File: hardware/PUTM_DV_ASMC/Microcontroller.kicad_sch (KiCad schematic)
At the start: 25 parts, among them U5 LM4040C33FTA, U6 STM32G484RETx

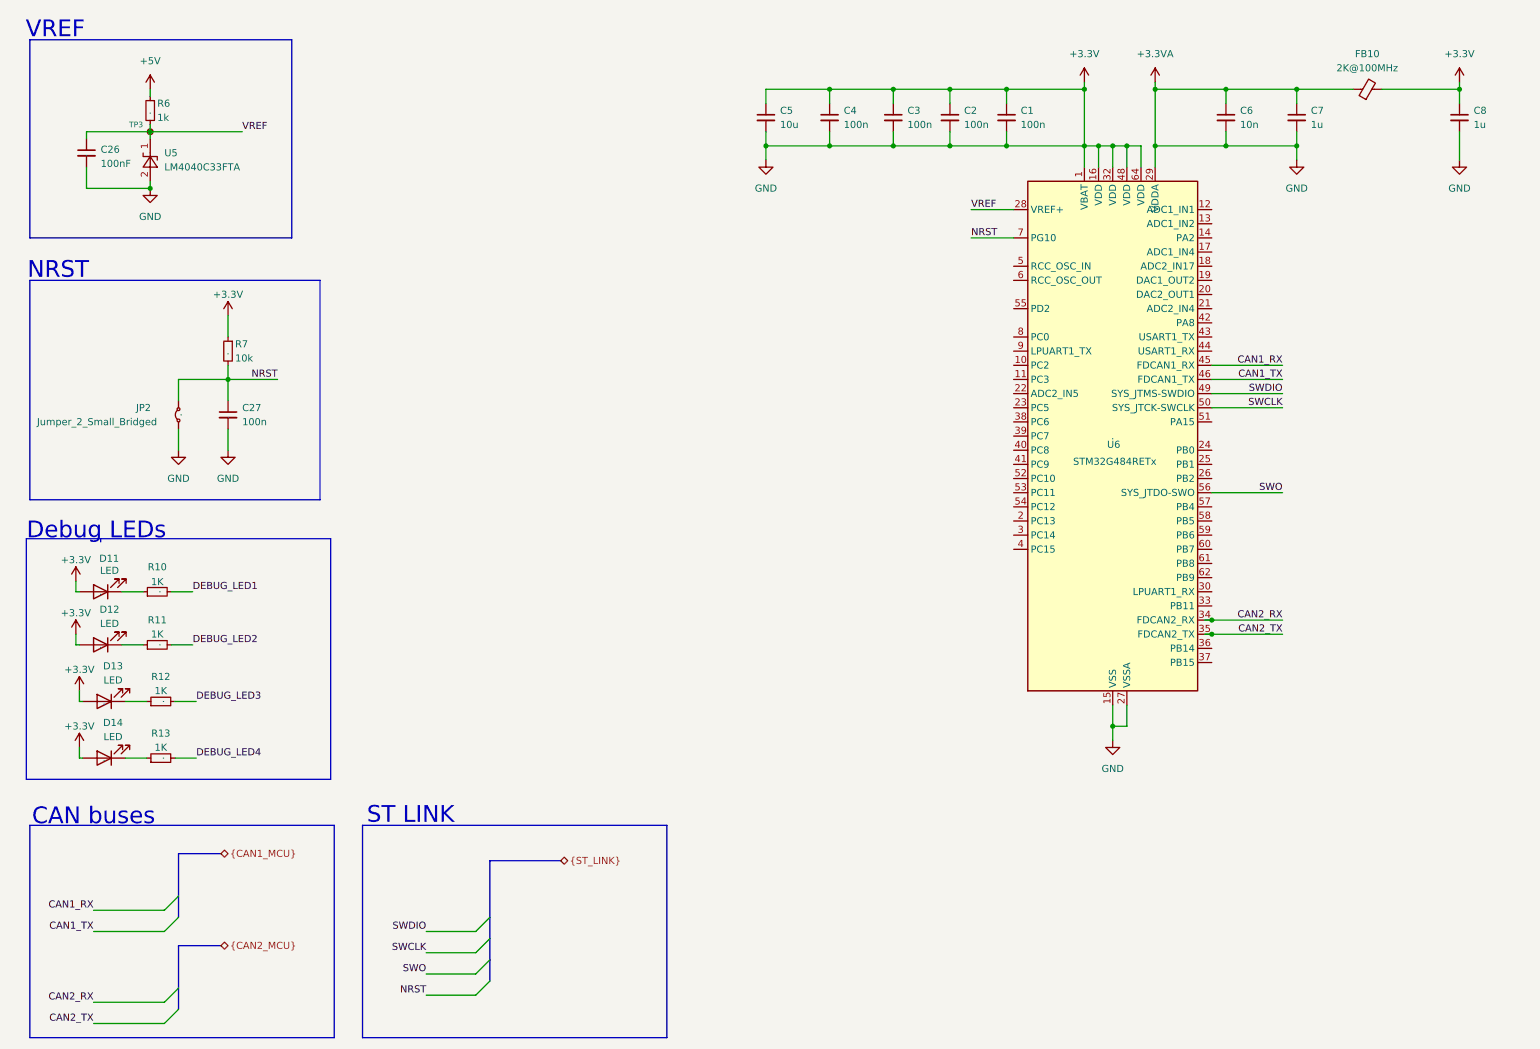
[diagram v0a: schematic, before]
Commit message: schematics without main connector
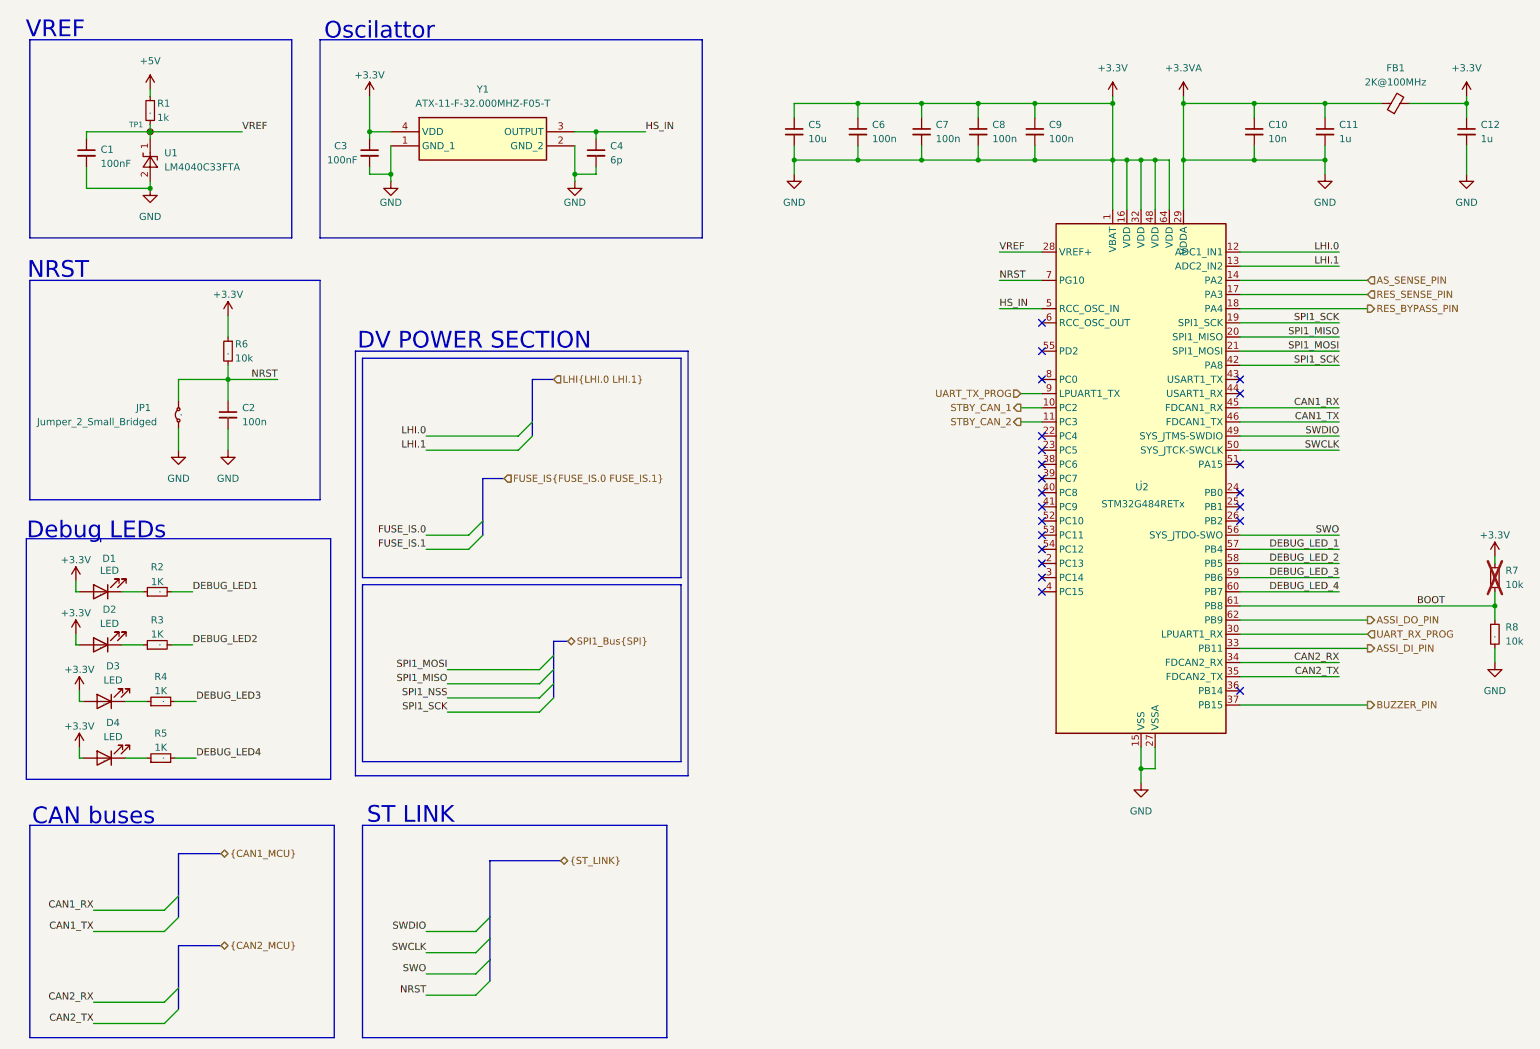
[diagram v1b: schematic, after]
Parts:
- added C3: 100nF, Capacitor_SMD:C_0603_1608Metric_Pad1.08x0.95mm_HandSolder, symbol Device:C_Small
- added C4: 6p, Capacitor_SMD:C_0603_1608Metric_Pad1.08x0.95mm_HandSolder, symbol Device:C_Small
- added R7, R8: 10k, Resistor_SMD:R_0603_1608Metric, symbol Device:R_Small
- added Y1: ATX-11-F-32.000MHZ-F05-T, Samacsys:ATX11F32000MHZF05T, symbol Samacsys:ATX-11-F-32.000MHZ-F05-T
- renumbered C26 to C1, C6 to C10, C7 to C11, C8 to C12, C27 to C2, C4 to C6, C3 to C7, C2 to C8, C1 to C9, D11 to D1, D12 to D2, D13 to D3, D14 to D4, FB10 to FB1, JP2 to JP1, R6 to R1, R10 to R2, R11 to R3, R12 to R4, R13 to R5, R7 to R6, TP3 to TP1, U5 to U1, U6 to U2
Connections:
- net +3.3V: now also C3.1, C3.2, C4.2, R7.1, R8.2, Y1.1 (GND_1), Y1.2 (GND_2), Y1.4 (VDD)
- net STBY_CAN_1: now reaches U2.10 (PC2)
- net STBY_CAN_2: now reaches U2.11 (PC3)
- net LHI.0: now reaches U2.12 (PA0)
- net LHI.1: now reaches U2.13 (PA1)
- net AS_SENSE_PIN: now reaches U2.14 (PA2)
- net RES_SENSE_PIN: now reaches U2.17 (PA3)
- net RES_BYPASS_PIN: now reaches U2.18 (PA4)
- net SPI1_SCK: now reaches U2.19 (PA5)
- net SPI1_SCK: now also U2.42 (PA8)
- net SPI1_MISO: now reaches U2.20 (PA6)
- net SPI1_MOSI: now reaches U2.21 (PA7)
- net UART_RX_PROG: now reaches U2.30 (PB10)
- net ASSI_DI_PIN: now reaches U2.33 (PB11)
- net BUZZER_PIN: now reaches U2.37 (PB15)
- net HS_IN: now reaches U2.5 (PF0)
- net HS_IN: now also C4.1, Y1.3 (OUTPUT)
- net DEBUG_LED_1: now reaches U2.57 (PB4)
- net DEBUG_LED_2: now reaches U2.58 (PB5)
- net DEBUG_LED_3: now reaches U2.59 (PB6)
- net DEBUG_LED_4: now reaches U2.60 (PB7)
- net BOOT: now reaches U2.61 (PB8)
- net BOOT: now also R7.2, R8.1
- net ASSI_DO_PIN: now reaches U2.62 (PB9)
- net UART_TX_PROG: now reaches U2.9 (PC1)
- no-connect marks 0 -> 22
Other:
- note added: "DV POWER SECTION"
- note added: "Oscilattor"
- moved on the sheet: C10, C11, C12, C5, C6, C7, C8, C9, FB1, U2

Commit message: done schematic v1
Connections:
- net ADC: now reaches U2.24 (PB0)
- net GPIO: now reaches U2.25 (PB1)
- no-connect marks 22 -> 20
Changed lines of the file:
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@@
 	)
 	(no_connect
-		(at 233.68 101.6)
-	)
-	(no_connect
 		(at 233.68 78.74)
 	)
@@
 	)
 	(no_connect
-		(at 233.68 99.06)
-	)
-	(no_connect
 		(at 198.12 111.76)
 	)
@@
 	(wire
 		(pts
+			(xy 233.68 99.06) (xy 256.54 99.06)
+		)
+		(stroke
+			(width 0)
+			(type default)
+		)
+	)
+	(wire
+		(pts
 			(xy 42.545 146.685) (xy 46.355 146.685)
 		)
@@
 	(wire
 		(pts
+			(xy 233.68 101.6) (xy 256.54 101.6)
+		)
+		(stroke
+			(width 0)
+			(type default)
+		)
+	)
+	(wire
+		(pts
 			(xy 38.1 35.56) (xy 38.1 34.29)
 		)
@@
 		)
 	)
+	(hierarchical_label "ADC"
+		(shape bidirectional)
+		(at 256.54 99.06 0)
+		(effects
+			(font
+				(size 1.27 1.27)
+			)
+			(justify left)
+		)
+	)
 	(hierarchical_label "RES_BYPASS_PIN"
 		(shape output)
@@
 	)
 	(hierarchical_label "ASSI_DI_PIN"
-		(shape output)
+		(shape bidirectional)
 		(at 256.54 127 0)
 		(effects
@@
 		)
 	)
+	(hierarchical_label "GPIO"
+		(shape bidirectional)
+		(at 256.54 101.6 0)
+		(effects
+			(font
+				(size 1.27 1.27)
+			)
+			(justify left)
+		)
+	)
 	(hierarchical_label "UART_RX_PROG"
 		(shape input)
@@
 		)
 		(property "Value" "STM32G484RETx"
-			(at 208.788 101.092 0)
+			(at 208.788 96.012 0)
 			(show_name no)
 			(do_not_autoplace no)
@@
 		)
 		(pin "25"
+			(alternate "ADC3_IN1")
 		)
 		(pin "56"

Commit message: schematic without error
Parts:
- Y1: footprint Samacsys:ATX11F32000MHZF05T -> ATX11F32000MHZF05T:ATX11F32000MHZF05T
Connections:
- net DEBUG_LED1 is gone; now on net DEBUG_LED_1: R2.2
- net DEBUG_LED2 is gone; now on net DEBUG_LED_2: R3.2
- net DEBUG_LED3 is gone; now on net DEBUG_LED_3: R4.2
- net DEBUG_LED4 is gone; now on net DEBUG_LED_4: R5.2
- net SPI1_NSS: now also U2.42 (PA8)
- net SPI1_SCK: no longer U2.42 (PA8)
- net FUSE_ISO.0: now reaches U2.40 (PC8)
- net FUSE_ISO.1: now reaches U2.41 (PC9)
- no-connect marks 20 -> 18
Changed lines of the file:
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@@
 	(rectangle
 		(start 74.93 73.66)
-		(end 134.62 149.86)
+		(end 137.16 149.86)
 		(stroke
 			(width 0)
@@
 	(rectangle
 		(start 76.2 115.57)
-		(end 133.35 147.32)
+		(end 135.89 147.32)
 		(stroke
 			(width 0)
@@
 	(rectangle
 		(start 76.2 74.93)
-		(end 133.35 114.3)
+		(end 135.89 114.3)
 		(stroke
 			(width 0)
@@
 	)
 	(no_connect
-		(at 198.12 101.6)
-	)
-	(no_connect
-		(at 198.12 99.06)
-	)
-	(no_connect
 		(at 198.12 78.74)
 	)
@@
 	(wire
 		(pts
+			(xy 190.5 99.06) (xy 198.12 99.06)
+		)
+		(stroke
+			(width 0)
+			(type default)
+		)
+	)
+	(wire
+		(pts
 			(xy 25.4 144.78) (xy 25.4 146.685)
 		)
@@
 	(wire
 		(pts
+			(xy 190.5 101.6) (xy 198.12 101.6)
+		)
+		(stroke
+			(width 0)
+			(type default)
+		)
+	)
+	(wire
+		(pts
 			(xy 26.035 146.685) (xy 25.4 146.685)
 		)
@@
 		)
 	)
+	(label "FUSE_ISO.0"
+		(at 190.5 99.06 180)
+		(effects
+			(font
+				(size 1.27 1.27)
+			)
+			(justify right bottom)
+		)
+	)
 	(label "CAN1_RX"
 		(at 27.94 173.99 180)
@@
 		)
 	)
-	(label "DEBUG_LED4"
+	(label "DEBUG_LED_4"
 		(at 46.355 146.685 0)
 		(effects
@@
 		)
 	)
-	(label "FUSE_IS.0"
+	(label "FUSE_ISO.0"
 		(at 87.63 106.68 180)
 		(effects
@@
 		)
 	)
-	(label "SPI1_SCK"
+	(label "SPI1_NSS"
 		(at 251.46 76.2 180)
 		(effects
@@
 		)
 	)
-	(label "DEBUG_LED1"
+	(label "DEBUG_LED_1"
 		(at 45.72 116.84 0)
 		(effects
@@
 		)
 	)
+	(label "FUSE_ISO.1"
+		(at 190.5 101.6 180)
+		(effects
+			(font
+				(size 1.27 1.27)
+			)
+			(justify right bottom)
+		)
+	)
 	(label "CAN2_TX"
 		(at 27.94 194.31 180)
@@
 		)
 	)
-	(label "DEBUG_LED3"
+	(label "DEBUG_LED_3"
 		(at 46.355 136.525 0)
 		(effects
@@
 		)
 	)
-	(label "FUSE_IS.1"
+	(label "FUSE_ISO.1"
 		(at 87.63 109.22 180)
 		(effects
@@
 		)
 	)
-	(label "DEBUG_LED2"
+	(label "DEBUG_LED_2"
 		(at 45.72 126.365 0)
 		(effects
@@
 		)
 	)
-	(hierarchical_label "FUSE_IS{FUSE_IS.0 FUSE_IS.1}"
+	(hierarchical_label "FUSE_ISO{FUSE_ISO.0 FUSE_ISO.1}"
 		(shape input)
 		(at 101.6 96.52 0)
@@
 			)
 		)
-		(property "Footprint" "Samacsys:ATX11F32000MHZF05T"
+		(property "Footprint" "ATX11F32000MHZF05T:ATX11F32000MHZF05T"
 			(at 110.49 129.21 0)
 			(hide yes)

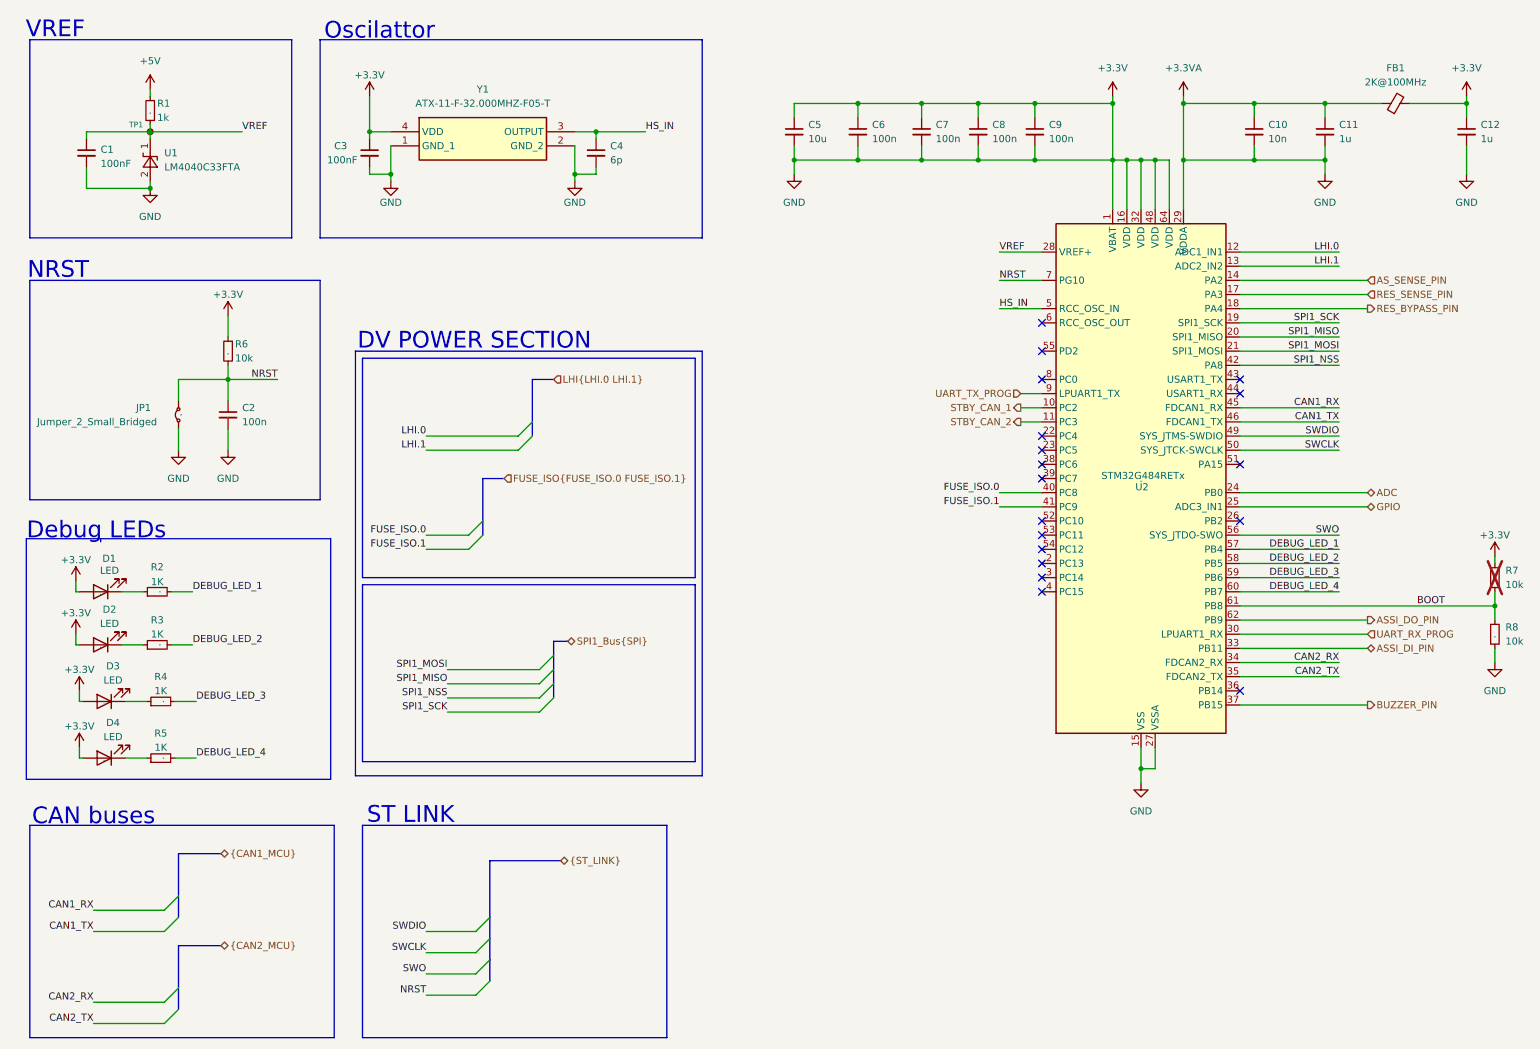
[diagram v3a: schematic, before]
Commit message: tylko dwa bledy z can - schemat na wykonczeniu
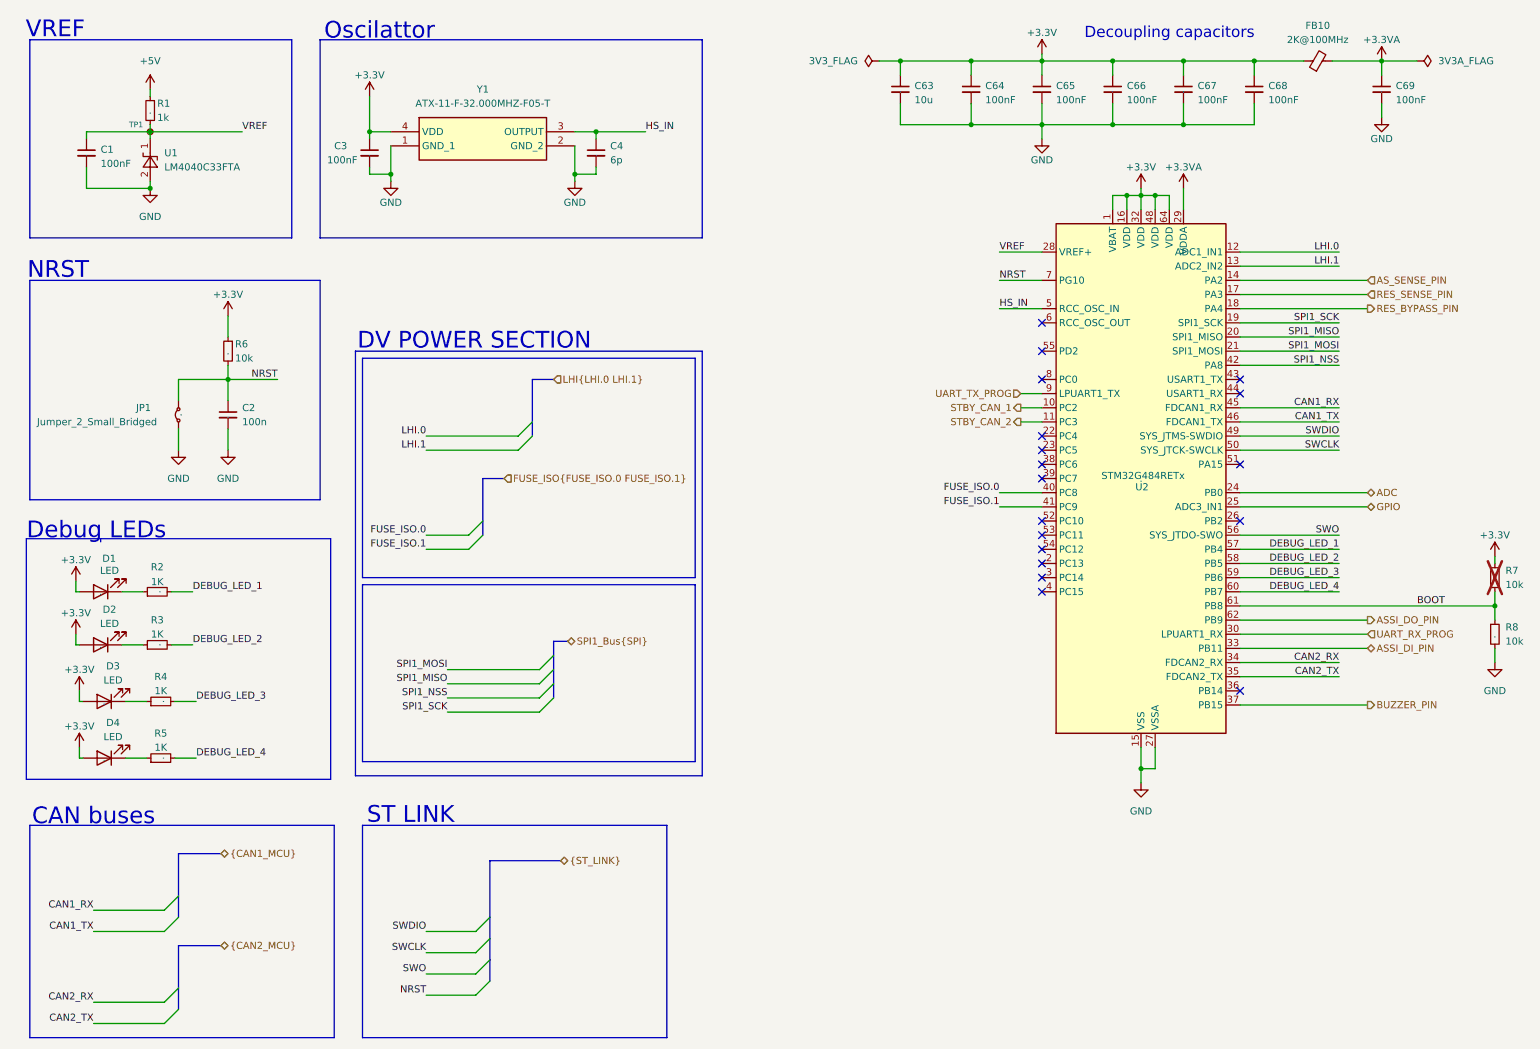
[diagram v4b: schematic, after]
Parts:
- removed C10: 10n, symbol Device:C_Small
- removed C11, C12: 1u, symbol Device:C_Small
- removed C5: 10u, symbol Device:C_Small
- removed C6, C7, C8, C9: 100n, symbol Device:C_Small
- removed FB1: 2K@100MHz, Inductor_SMD:L_0805_2012Metric_Pad1.05x1.20mm_HandSolder, symbol Device:FerriteBead_Small
- added C63: 10u, Capacitor_SMD:C_0805_2012Metric_Pad1.18x1.45mm_HandSolder, symbol Device:C_Small
- added C64, C65, C66, C67, C68, C69: 100nF, Capacitor_SMD:C_0603_1608Metric_Pad1.08x0.95mm_HandSolder, symbol Device:C_Small
- added FB10: 2K@100MHz, Inductor_SMD:L_0805_2012Metric_Pad1.05x1.20mm_HandSolder, symbol Device:FerriteBead_Small
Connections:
- net +3.3V: now also C63.1, C64.1, C65.1, C66.1, C67.1, C68.1, FB10.1; no longer C1.2, C2.2, C3.2, C4.2, JP1.1 (A), R8.2, U1.2 (A), U2.15 (VSS), U2.27 (VSSA), U2.29 (VDDA), U2.31 (VSS), U2.47 (VSS), U2.63 (VSS), Y1.1 (GND_1), Y1.2 (GND_2)
- new net +3.3VA: C69.1, FB10.2, U2.29 (VDDA)
- new net GND: C1.2, C2.2, C3.2, C4.2, C63.2, C64.2, C65.2, C66.2, C67.2, C68.2, C69.2, JP1.1 (A), R8.2, U1.2 (A), U2.15 (VSS), U2.27 (VSSA), U2.31 (VSS), U2.47 (VSS), U2.63 (VSS), Y1.1 (GND_1), Y1.2 (GND_2)
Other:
- note added: "Decoupling capacitors"
